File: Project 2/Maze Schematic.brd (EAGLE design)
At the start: 152.4 x 165.1 mm, 23 parts, among them SW1 BUTTON, SW2 BUTTON, SW3 BUTTON, SW4 BUTTON, SW5 BUTTON, U1 MOD-LED8X8RGB-CONN, U3 POCKETBEAGLE, U6 MOD-LED8X8RGB-CONN

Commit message: Renamed folder to project 2 and updated board layout
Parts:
- removed U$2: BUZZER, Buzzer Box:BUZZER-12MM
- removed U$3, U$8, U$9: LTST-C191TBKT, Buzzer Box:LED-SMD
- added BZZR1: BUZZER, Buzzer Box:BUZZER-12MM
- added C1, C2, C3: .1uF, Buzzer Box:C0603
- added C4: 10nF, Buzzer Box:C0603
- added LED1, LED2, LED3: LTST-C191TBKT, Buzzer Box:LED-SMD
- added R10, R11, R7, R8, R9: 1K, Buzzer Box:R0603
- added R6: 10K, Buzzer Box:R0603
- U2: value (none) -> MPU-9250
- moved R5 412.2 mm to (17.8, 36.8), turned to 90 degrees
- moved SW5 396.8 mm to (25.4, 31.8)
- moved R4 366.7 mm to (17.8, 11.4), turned to 90 degrees
- moved R3 361.2 mm to (33.0, 24.1), turned to 90 degrees
- moved SW4 351.3 mm to (25.4, 6.35)
- moved SW3 345.8 mm to (40.6, 19.1)
- moved R2 337.5 mm to (2.54, 24.1), turned to 90 degrees
- moved SW_PWR 330.1 mm to (144.8, 125.7)
- moved SW2 322.1 mm to (10.2, 19.1)
- moved R1 318.8 mm to (17.8, 24.1), turned to 90 degrees
- moved U6 302.5 mm to (25.4, 81.3), turned to 90 degrees
- moved SW1 257.6 mm to (25.4, 19.1)
- moved U1 175.8 mm to (25.4, 143.5), turned to 90 degrees
- moved U2 149.9 mm to (76.2, 82.5)
- moved U3 132.3 mm to (87.6, 2.54)
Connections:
- removed net N$2: U2.P$21, U3.26
- removed net N$3: U2.P$18, U3.22
- new net BUZZER: BZZR1.+, U3.37
- new net I2C2_SCL: R10.1, U2.P$23, U3.28
- new net I2C2_SDA: R11.1, U2.P$24, U3.26
- new net LED-ARRAY1_CS: U3.67, U6.3
- new net LED-ARRAY1_MOSI: U3.12, U6.4
- new net LED-ARRAY1_SCLK: U3.65, U6.2
- new net LED-ARRAY2_CS: U1.3, U3.6
- new net LED-ARRAY2_MOSI: U1.4, U3.61
- new net LED-ARRAY2_SCLK: U1.2, U3.8
- new net LED1: R7.2, U3.44
- new net LED2: R8.2, U3.56
- new net LED3: R9.2, U3.53
- new net MPU_INT: U2.P$12, U3.46
- new net N$4: C1.1, R6.1, SW_PWR.P$3, SW_PWR.P$4, U3.48
- new net N$5: LED1.A(+), R7.1
- new net N$6: LED2.A(+), R8.1
- new net N$7: LED3.A(+), R9.1
- new net VDD_3P3V: C3.1, C4.1, R10.2, R11.2, U2.P$1, U2.P$13, U2.P$22, U2.P$8, U3.14, U3.59
- new net VDD_5V: U1.1, U3.24, U3.49, U6.1
- net BTN1: now also U3.20
- net BTN2: now also U3.55
- net BTN3: now also U3.58
- net BTN4: now also U3.54
- net BTN5: now also U3.60
- net GND: now also BZZR1.-, C1.2, C2.2, C3.2, C4.2, LED1.C(-), LED2.C(-), LED3.C(-), SW_PWR.P$1, SW_PWR.P$2, U1.5, U1.6, U2.P$18, U2.P$20, U2.P$9, U3.15, U3.16, U3.22, U3.51, U3.57, U6.5, U6.6
- net N$1: now also C2.1, U2.P$10; no longer U2.P$7, U3.28

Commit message: Began routing and updated pocket beagle device
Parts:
- moved R8 61.1 mm to (68.6, 7.87)
- moved R9 61.1 mm to (68.6, 4.06)
- moved LED2 61.1 mm to (64.8, 7.87)
- moved LED3 61.1 mm to (64.8, 4.06)
- moved R7 60.7 mm to (68.6, 11.4)
- moved LED1 60.7 mm to (64.8, 11.4)
- moved R2 0.51 mm to (3.05, 24.1)
- moved R1 0.51 mm to (18.3, 24.1)
- moved R4 0.51 mm to (18.3, 11.4)
- moved R5 0.51 mm to (18.3, 36.8)
- moved R3 0.51 mm to (33.5, 24.1)
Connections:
- removed net SYS_VDD1_3P3V: R1.2, R2.2, R3.2, R4.2, R5.2
- net LED-ARRAY1_MOSI: now also U3.61; no longer U3.12
- net LED-ARRAY2_MOSI: now also U3.12; no longer U3.61
- net VDD_3P3V: now also R1.2, R2.2, R3.2, R4.2, R5.2
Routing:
- net VDD_3P3V: track 0.00 -> 6.16 mm, vias 0 -> 5
- net GND: track 0.00 -> 3.41 mm, vias 0 -> 3
- net BTN3: track 0.00 -> 2.14 mm
- net BTN4: track 0.00 -> 2.14 mm
- net BTN2: track 0.00 -> 2.14 mm
- net BTN1: track 0.00 -> 2.14 mm
- net BTN5: track 0.00 -> 2.14 mm
- net N$7: track 0.00 -> 1.86 mm
- net N$6: track 0.00 -> 1.86 mm
- net N$5: track 0.00 -> 1.86 mm

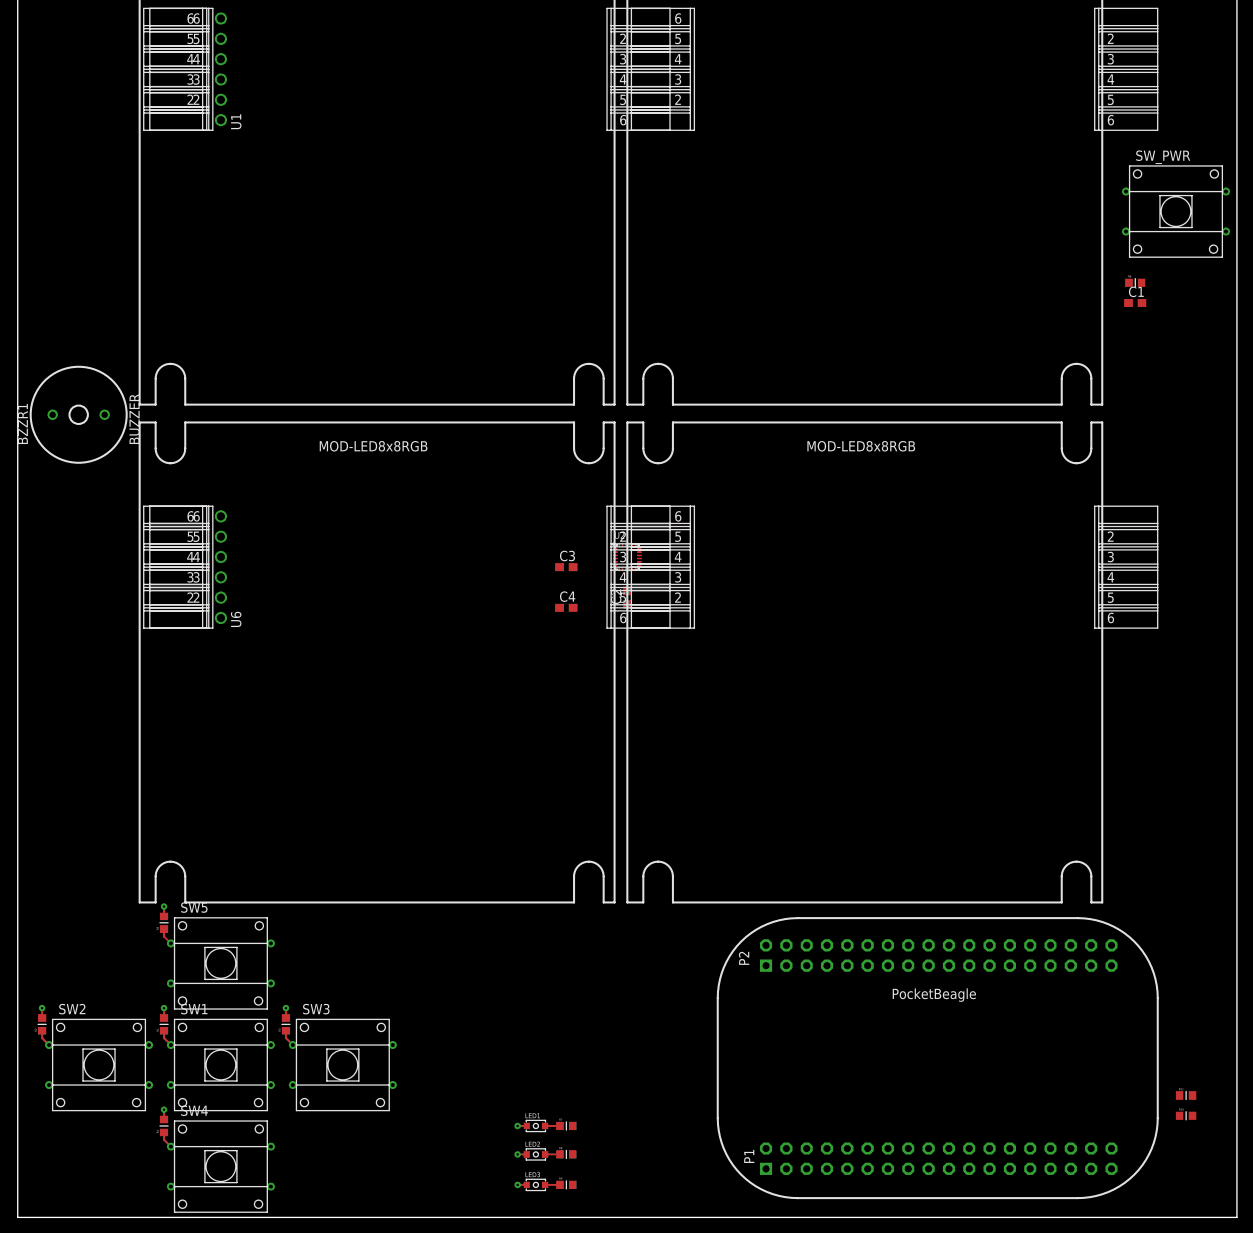
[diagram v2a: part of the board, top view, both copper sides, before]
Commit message: Completed board routing
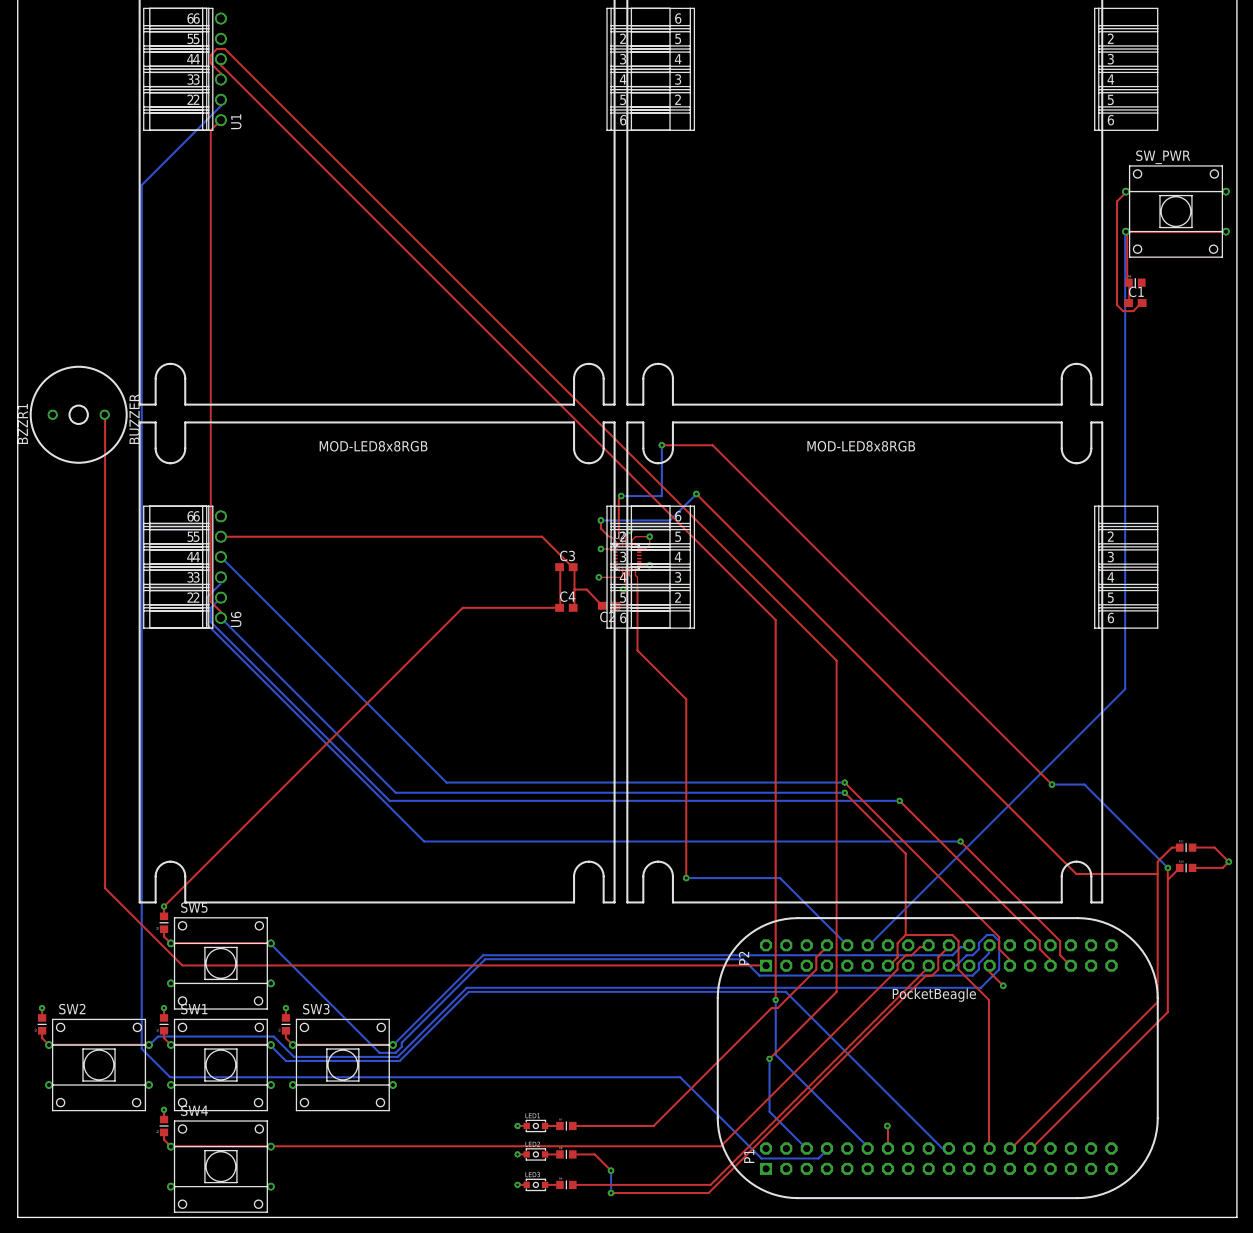
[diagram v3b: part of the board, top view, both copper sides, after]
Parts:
- moved R10 31.0 mm to (146.1, 43.7)
- moved R11 31.0 mm to (146.1, 46.2)
- moved C2 2.50 mm to (73.9, 76.5), turned to 180 degrees
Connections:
- net N$1 renamed REGOUT
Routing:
- net LED-ARRAY2_SCLK: track 0.00 -> 214.7 mm
- net VDD_5V: track 0.00 -> 210.6 mm, vias 0 -> 1
- net LED-ARRAY2_CS: track 0.00 -> 180.2 mm, vias 0 -> 1
- net LED-ARRAY2_MOSI: track 0.00 -> 169.9 mm, vias 0 -> 1
- net I2C2_SCL: track 0.00 -> 147.4 mm, vias 0 -> 4
- net BUZZER: track 0.00 -> 145.9 mm
- net I2C2_SDA: track 0.00 -> 141.9 mm, vias 0 -> 2
- net BTN2: track 2.14 -> 139.1 mm
- net LED-ARRAY1_CS: track 0.00 -> 133.3 mm, vias 0 -> 1
- net LED-ARRAY1_SCLK: track 0.00 -> 127.4 mm, vias 0 -> 1
- net N$4: track 0.00 -> 124.4 mm
- net LED-ARRAY1_MOSI: track 0.00 -> 121.1 mm, vias 0 -> 1
- net BTN5: track 2.14 -> 118.7 mm
- net BTN1: track 2.14 -> 112.0 mm
- net BTN4: track 2.14 -> 107.8 mm
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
